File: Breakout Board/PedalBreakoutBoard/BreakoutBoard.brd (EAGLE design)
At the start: 69.5 x 63.5 mm, 36 parts

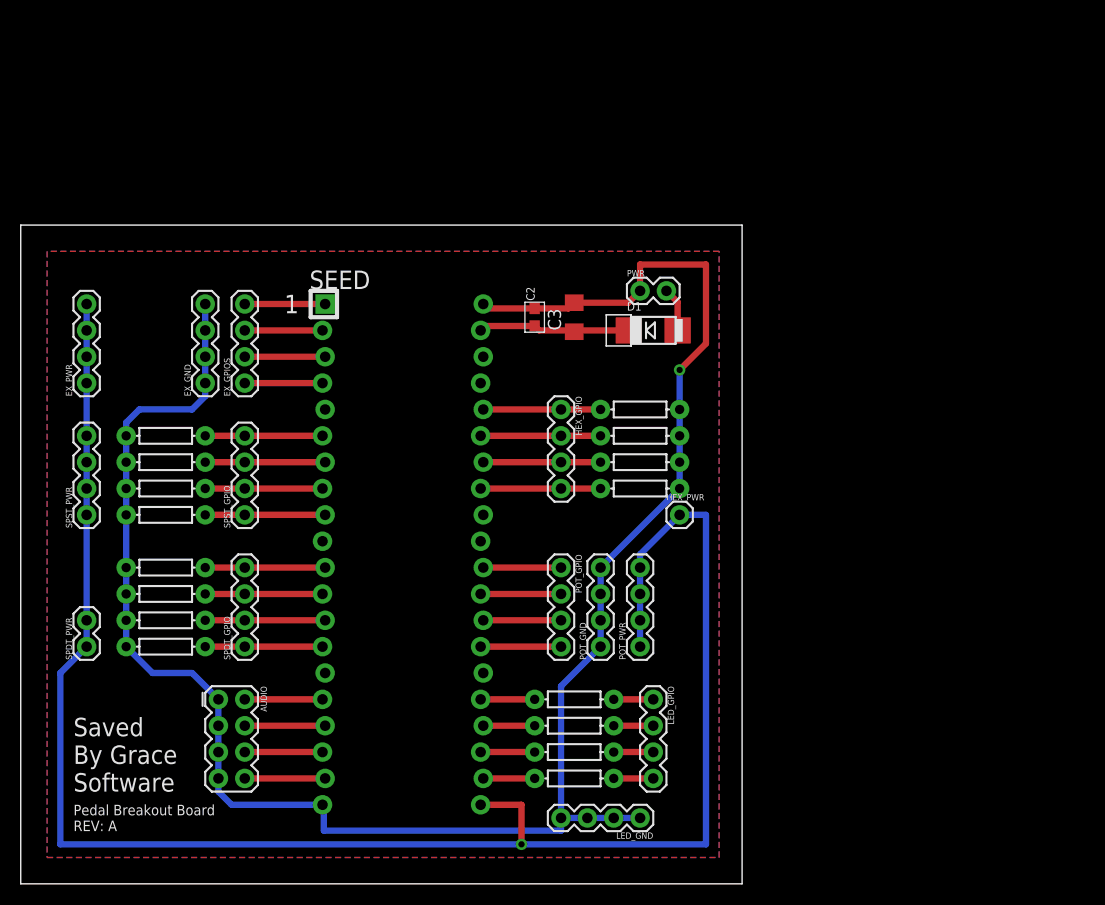
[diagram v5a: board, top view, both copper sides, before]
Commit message: DP-16 - Updating to through hole parts
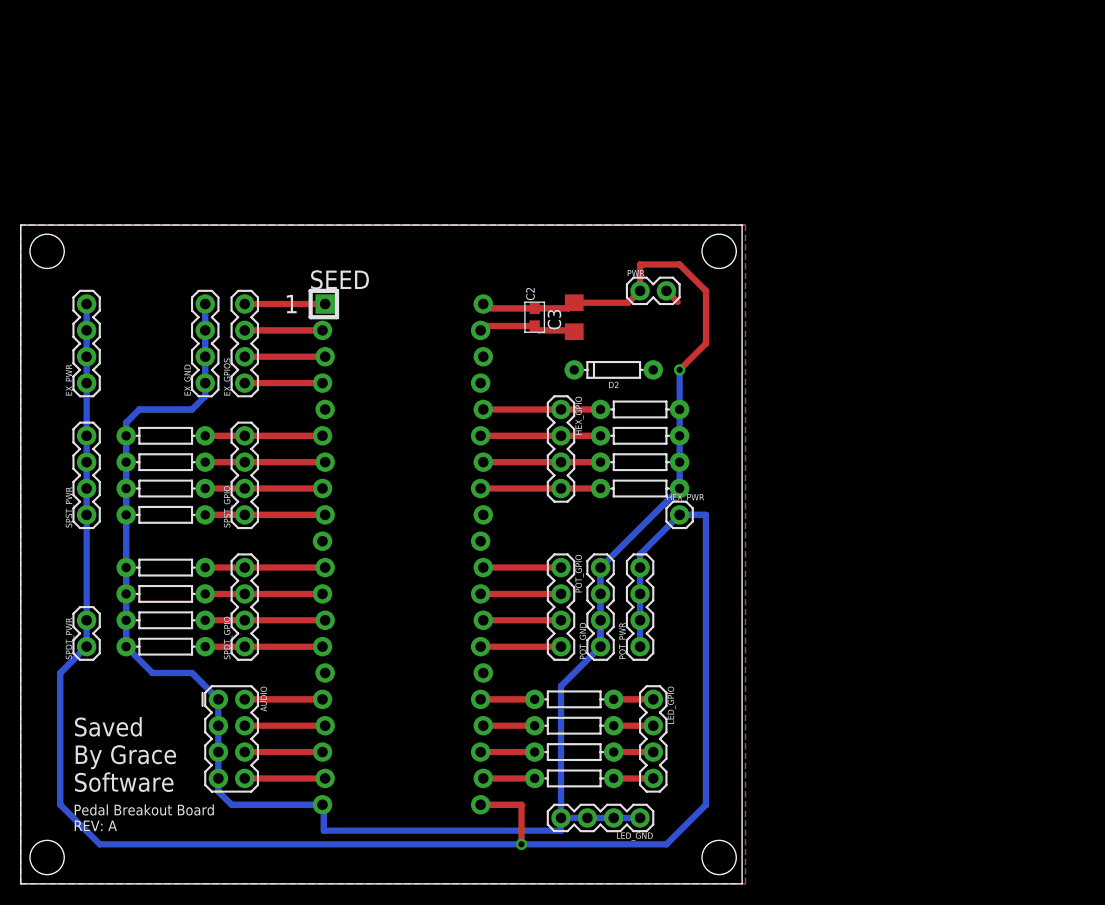
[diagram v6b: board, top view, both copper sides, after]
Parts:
- removed D1: S1B, Electrosmith-Semiconductors:SMADIODE
- added D2: 200mA/100V/1V, SparkFun-DiscreteSemi:DIODE-1N4148
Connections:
- net +9V_IN: now also D2.C; no longer D1.C
- net N$2: now also D2.A; no longer D1.A
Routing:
- net +9V_IN: track 14.8 -> 9.68 mm
- net +3V3_A: track 171.7 -> 167.2 mm
- net N$2: track 4.26 -> 1.53 mm
- net GND: track 187.8 -> 186.4 mm
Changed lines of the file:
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@@
 By Grace
 Software</text>
+<hole x="0" y="58.42" drill="3.302"/>
+<hole x="64.77" y="58.42" drill="3.302"/>
+<hole x="64.77" y="0" drill="3.302"/>
+<hole x="0" y="0" drill="3.302"/>
 </plain>
 <attributes>
@@
 <attribute name="VALUE" x="53.34" y="50.8" size="1.27" layer="27" rot="R90"/>
 </element>
-<element name="D1" library="Electrosmith-Semiconductors" package="SMADIODE" value="S1B" x="58.42" y="50.8" smashed="yes">
-<attribute name="BIN#" value="12-006" x="74.93" y="-10.16" size="1.778" layer="27" display="off"/>
-<attribute name="IPN" value="S1B" x="74.93" y="-10.16" size="1.778" layer="27" display="off"/>
-<attribute name="MPN" value="S1B" x="74.93" y="-10.16" size="1.778" layer="27" display="off"/>
-<attribute name="NAME" x="55.88" y="52.705" size="0.8128" layer="25" font="vector"/>
-<attribute name="PACKAGE" value="SMA" x="74.93" y="-10.16" size="1.778" layer="27" display="off"/>
-<attribute name="VALUE" x="55.88" y="48.03775" size="0.8128" layer="27" font="vector"/>
-</element>
 <element name="L1" library="SparkFun-Resistors" library_urn="urn:adsk.eagle:library:532" package="AXIAL-0.3" package3d_urn="urn:adsk.eagle:package:39658/1" value="330" x="50.8" y="15.24" smashed="yes">
 <attribute name="PROD_ID" value="RES-8371" x="83.82" y="-44.45" size="1.778" layer="27" display="off"/>
@@
 <attribute name="PROD_ID" value="CONN-09696" x="15.24" y="45.72" size="1.778" layer="27" rot="R90" display="off"/>
 <attribute name="VALUE" x="17.272" y="44.45" size="0.6096" layer="27" font="vector" ratio="20" rot="R90"/>
+</element>
+<element name="D2" library="SparkFun-DiscreteSemi" library_urn="urn:adsk.eagle:library:514" package="DIODE-1N4148" package3d_urn="urn:adsk.eagle:package:38452/1" value="200mA/100V/1V" x="54.61" y="46.99" smashed="yes" rot="R180">
+<attribute name="NAME" x="54.61" y="45.847" size="0.6096" layer="25" font="vector" ratio="20" rot="R180" align="bottom-center"/>
+<attribute name="PROD_ID" value="DIO-08378" x="54.61" y="46.99" size="1.778" layer="27" rot="R180" display="off"/>
+<attribute name="VALUE" x="54.61" y="48.133" size="0.6096" layer="27" font="vector" ratio="20" rot="R180" align="top-center"/>
 </element>
 </elements>
@@
 <wire x1="46.99" y1="52.92" x2="42.457" y2="52.92" width="0.6096" layer="1"/>
 <wire x1="42.457" y1="52.92" x2="42.037" y2="53.34" width="0.6096" layer="1"/>
-<wire x1="60.96" y1="46.99" x2="63.5" y2="49.53" width="0.6096" layer="1"/>
-<wire x1="63.5" y1="49.53" x2="63.5" y2="57.15" width="0.6096" layer="1"/>
-<wire x1="63.5" y1="57.15" x2="57.15" y2="57.15" width="0.6096" layer="1"/>
-<wire x1="57.15" y1="57.15" x2="57.15" y2="54.61" width="0.6096" layer="1"/>
+<wire x1="63.5" y1="49.53" x2="60.96" y2="46.99" width="0.6096" layer="1"/>
+<wire x1="57.15" y1="54.61" x2="57.15" y2="57.15" width="0.6096" layer="1"/>
 <polygon width="0.1524" layer="1" isolate="0.3048">
-<vertex x="64.77" y="0"/>
-<vertex x="64.77" y="58.42"/>
-<vertex x="0" y="58.42"/>
-<vertex x="0" y="0"/>
+<vertex x="67.31" y="-2.54"/>
+<vertex x="67.31" y="60.96"/>
+<vertex x="-2.54" y="60.96"/>
+<vertex x="-2.54" y="-2.54"/>
 </polygon>
 <polygon width="0.1524" layer="16" isolate="0.3048">
-<vertex x="0" y="58.42"/>
-<vertex x="0" y="0"/>
-<vertex x="64.77" y="0"/>
-<vertex x="64.77" y="58.42"/>
+<vertex x="-2.54" y="60.96"/>
+<vertex x="-2.54" y="-2.54"/>
+<vertex x="67.31" y="-2.54"/>
+<vertex x="67.31" y="60.96"/>
 </polygon>
+<wire x1="57.15" y1="57.15" x2="60.96" y2="57.15" width="0.6096" layer="1"/>
+<wire x1="60.96" y1="57.15" x2="63.5" y2="54.61" width="0.6096" layer="1"/>
+<wire x1="63.5" y1="54.61" x2="63.5" y2="49.53" width="0.6096" layer="1"/>
 </signal>
 <signal name="SPST1">
@@
 <wire x1="3.81" y1="38.1" x2="3.81" y2="40.64" width="0.6096" layer="16"/>
 <wire x1="3.81" y1="20.32" x2="1.27" y2="17.78" width="0.6096" layer="16"/>
-<wire x1="1.27" y1="17.78" x2="1.27" y2="1.27" width="0.6096" layer="16"/>
-<wire x1="63.5" y1="1.27" x2="63.5" y2="33.02" width="0.6096" layer="16"/>
+<wire x1="1.27" y1="5.08" x2="1.27" y2="17.78" width="0.6096" layer="16"/>
+<wire x1="63.5" y1="5.08" x2="63.5" y2="33.02" width="0.6096" layer="16"/>
 <wire x1="60.96" y1="33.02" x2="63.5" y2="33.02" width="0.6096" layer="16"/>
 <wire x1="60.96" y1="33.02" x2="57.15" y2="29.21" width="0.6096" layer="16"/>
@@
 <wire x1="45.72" y1="5.08" x2="45.72" y2="1.27" width="0.6096" layer="1"/>
 <via x="45.72" y="1.27" extent="1-16" drill="0.6"/>
-<wire x1="45.72" y1="1.27" x2="63.5" y2="1.27" width="0.6096" layer="16"/>
-<wire x1="1.27" y1="1.27" x2="45.72" y2="1.27" width="0.6096" layer="16"/>
+<wire x1="45.72" y1="1.27" x2="59.69" y2="1.27" width="0.6096" layer="16"/>
+<wire x1="45.72" y1="1.27" x2="5.08" y2="1.27" width="0.6096" layer="16"/>
 <wire x1="3.81" y1="40.64" x2="3.81" y2="45.72" width="0.6096" layer="16"/>
 <wire x1="3.81" y1="45.72" x2="3.81" y2="48.26" width="0.6096" layer="16"/>
 <wire x1="3.81" y1="48.26" x2="3.81" y2="50.8" width="0.6096" layer="16"/>
 <wire x1="3.81" y1="50.8" x2="3.81" y2="53.34" width="0.6096" layer="16"/>
+<wire x1="59.69" y1="1.27" x2="63.5" y2="5.08" width="0.6096" layer="16"/>
+<wire x1="5.08" y1="1.27" x2="1.27" y2="5.08" width="0.6096" layer="16"/>
 </signal>
 <signal name="SPDT1_1">
@@
 </signal>
 <signal name="N$2">
-<contactref element="D1" pad="A"/>
 <contactref element="PWR" pad="2"/>
 <wire x1="59.69" y1="54.61" x2="60.7695" y2="53.5305" width="0.6096" layer="1"/>
-<wire x1="60.7695" y1="53.5305" x2="60.7695" y2="50.8" width="0.6096" layer="1"/>
+<contactref element="D2" pad="A"/>
+<wire x1="58.42" y1="46.99" x2="60.7695" y2="53.5305" width="0" layer="19" extent="1-1"/>
 </signal>
 <signal name="+9V_IN">
@@
 <contactref element="C2" pad="1"/>
 <contactref element="C3" pad="1"/>
-<contactref element="D1" pad="C"/>
 <wire x1="50.8" y1="50.67" x2="50.93" y2="50.8" width="0.6096" layer="1"/>
-<wire x1="50.93" y1="50.8" x2="56.0705" y2="50.8" width="0.6096" layer="1"/>
 <wire x1="41.783" y1="50.8" x2="42.203" y2="51.22" width="0.6096" layer="1"/>
 <wire x1="42.203" y1="51.22" x2="46.99" y2="51.22" width="0.6096" layer="1"/>
 <wire x1="46.99" y1="51.22" x2="47.41" y2="50.8" width="0.6096" layer="1"/>
 <wire x1="47.41" y1="50.8" x2="50.93" y2="50.8" width="0.6096" layer="1"/>
+<contactref element="D2" pad="C"/>
+<wire x1="50.8" y1="50.67" x2="50.8" y2="46.99" width="0" layer="19" extent="1-1"/>
 </signal>
 <signal name="N$1">

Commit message: Working on adding mounting holes
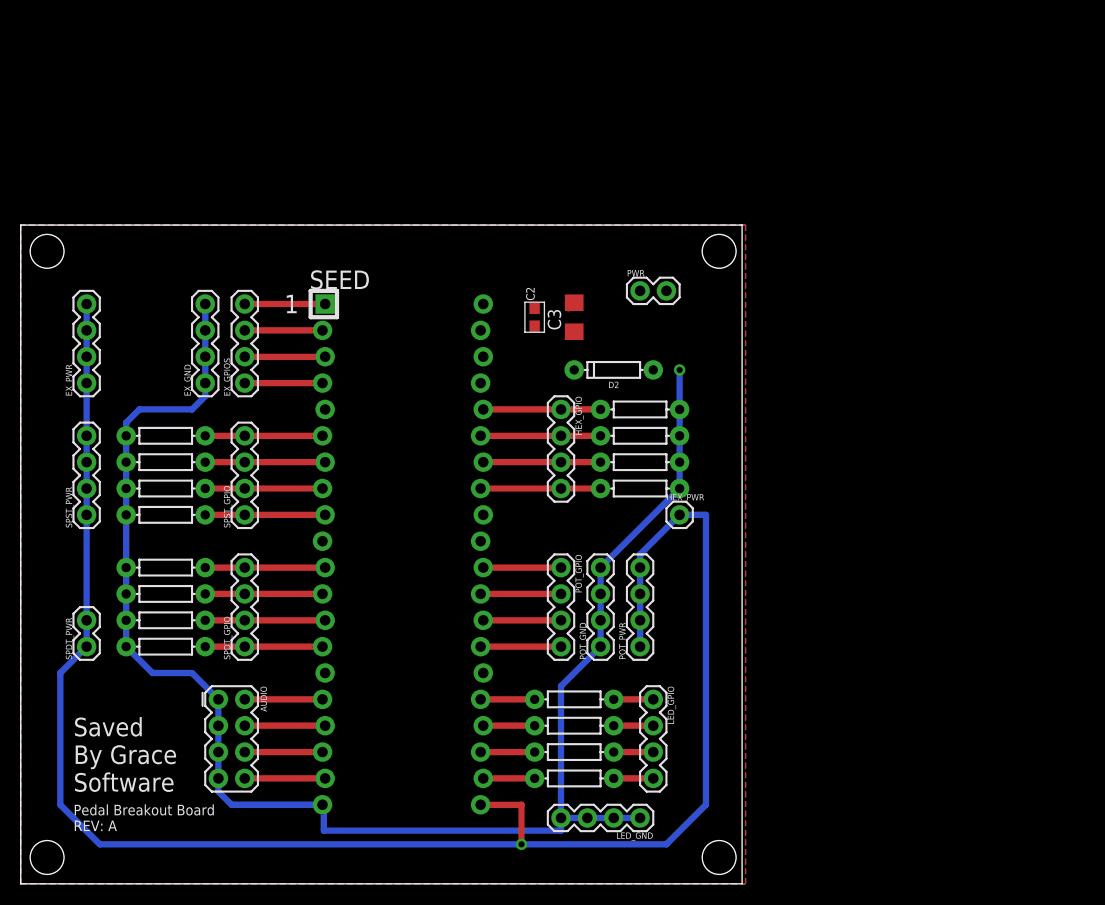
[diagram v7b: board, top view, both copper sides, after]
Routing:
- net GND: track 186.4 -> 153.1 mm
- net +9V_IN: track 9.68 -> 0.78 mm
- net N$2: track 1.53 -> 0.00 mm
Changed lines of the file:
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@@
 By Grace
 Software</text>
-<hole x="0" y="58.42" drill="3.302"/>
-<hole x="64.77" y="58.42" drill="3.302"/>
-<hole x="64.77" y="0" drill="3.302"/>
-<hole x="0" y="0" drill="3.302"/>
+<hole x="0" y="58.42" drill="3.2639"/>
+<hole x="64.77" y="58.42" drill="3.2639"/>
+<hole x="64.77" y="0" drill="3.2639"/>
+<hole x="0" y="0" drill="3.2639"/>
 </plain>
 <attributes>
@@
 <wire x1="60.96" y1="43.18" x2="60.96" y2="46.99" width="0.6096" layer="16"/>
 <via x="60.96" y="46.99" extent="1-16" drill="0.6"/>
-<wire x1="57.15" y1="54.61" x2="56.01" y2="53.47" width="0.6096" layer="1"/>
-<wire x1="56.01" y1="53.47" x2="50.8" y2="53.47" width="0.6096" layer="1"/>
 <wire x1="50.8" y1="53.47" x2="50.25" y2="52.92" width="0.6096" layer="1"/>
-<wire x1="50.25" y1="52.92" x2="46.99" y2="52.92" width="0.6096" layer="1"/>
-<wire x1="46.99" y1="52.92" x2="42.457" y2="52.92" width="0.6096" layer="1"/>
 <wire x1="42.457" y1="52.92" x2="42.037" y2="53.34" width="0.6096" layer="1"/>
-<wire x1="63.5" y1="49.53" x2="60.96" y2="46.99" width="0.6096" layer="1"/>
-<wire x1="57.15" y1="54.61" x2="57.15" y2="57.15" width="0.6096" layer="1"/>
 <polygon width="0.1524" layer="1" isolate="0.3048">
 <vertex x="67.31" y="-2.54"/>
@@
 <vertex x="67.31" y="60.96"/>
 </polygon>
-<wire x1="57.15" y1="57.15" x2="60.96" y2="57.15" width="0.6096" layer="1"/>
-<wire x1="60.96" y1="57.15" x2="63.5" y2="54.61" width="0.6096" layer="1"/>
-<wire x1="63.5" y1="54.61" x2="63.5" y2="49.53" width="0.6096" layer="1"/>
+<wire x1="50.8" y1="53.47" x2="57.15" y2="54.61" width="0" layer="19" extent="1-1"/>
+<wire x1="46.99" y1="52.92" x2="50.25" y2="52.92" width="0" layer="19" extent="1-1"/>
+<wire x1="42.457" y1="52.92" x2="46.99" y2="52.92" width="0" layer="19" extent="1-1"/>
+<wire x1="60.96" y1="46.99" x2="57.15" y2="54.61" width="0" layer="19" extent="1-1"/>
 </signal>
 <signal name="SPST1">
@@
 <signal name="N$2">
 <contactref element="PWR" pad="2"/>
-<wire x1="59.69" y1="54.61" x2="60.7695" y2="53.5305" width="0.6096" layer="1"/>
 <contactref element="D2" pad="A"/>
-<wire x1="58.42" y1="46.99" x2="60.7695" y2="53.5305" width="0" layer="19" extent="1-1"/>
+<wire x1="58.42" y1="46.99" x2="59.69" y2="54.61" width="0" layer="19" extent="1-1"/>
 </signal>
 <signal name="+9V_IN">
@@
 <wire x1="50.8" y1="50.67" x2="50.93" y2="50.8" width="0.6096" layer="1"/>
 <wire x1="41.783" y1="50.8" x2="42.203" y2="51.22" width="0.6096" layer="1"/>
-<wire x1="42.203" y1="51.22" x2="46.99" y2="51.22" width="0.6096" layer="1"/>
-<wire x1="46.99" y1="51.22" x2="47.41" y2="50.8" width="0.6096" layer="1"/>
-<wire x1="47.41" y1="50.8" x2="50.93" y2="50.8" width="0.6096" layer="1"/>
 <contactref element="D2" pad="C"/>
-<wire x1="50.8" y1="50.67" x2="50.8" y2="46.99" width="0" layer="19" extent="1-1"/>
+<wire x1="50.8" y1="46.99" x2="50.8" y2="50.67" width="0" layer="19" extent="1-1"/>
+<wire x1="46.99" y1="51.22" x2="50.8" y2="50.67" width="0" layer="19" extent="1-1"/>
+<wire x1="42.203" y1="51.22" x2="46.99" y2="51.22" width="0" layer="19" extent="1-1"/>
 </signal>
 <signal name="N$1">
